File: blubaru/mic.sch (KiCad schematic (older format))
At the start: 8 parts, among them J6 JACK_TRS_6PINS

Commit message: Put parts in the audio switch page.
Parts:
- renumbered C13 to C2, C14 to C3, C15 to C4, C16 to C5, C17 to C6, R9 to R1, R10 to R2
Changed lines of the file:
@@
 MIC_BIAS
 $Comp
-L C C16
+L C C5
 U 1 1 589D21D3
 P 5500 3750
-AR Path="/58AE7D2D/589D21D3" Ref="C16"  Part="1"
-AR Path="/58AEC2DA/58AE7D2D/589D21D3" Ref="C16"  Part="1"
-AR Path="/58B10FE0/58B1273D/58B189CE/58AE7D2D/589D21D3" Ref="C16"  Part="1"
-F 0 "C16" H 5525 3850 50  0000 L CNN
+F 0 "C5" H 5525 3850 50  0000 L CNN
 F 1 "47nF" H 5525 3650 50  0000 L CNN
 F 2 "" H 5538 3600 50  0000 C CNN
@@
 $EndComp
 $Comp
-L C C15
+L C C4
 U 1 1 589D223D
 P 5150 4100
-AR Path="/58AE7D2D/589D223D" Ref="C15"  Part="1"
-AR Path="/58AEC2DA/58AE7D2D/589D223D" Ref="C15"  Part="1"
-AR Path="/58B10FE0/58B1273D/58B189CE/58AE7D2D/589D223D" Ref="C15"  Part="1"
-F 0 "C15" H 5175 4200 50  0000 L CNN
+F 0 "C4" H 5175 4200 50  0000 L CNN
 F 1 "47nF" H 5175 4000 50  0000 L CNN
 F 2 "" H 5188 3950 50  0000 C CNN
@@
 $EndComp
 $Comp
-L C C17
+L C C6
 U 1 1 589D230D
 P 5500 4100
-AR Path="/58AE7D2D/589D230D" Ref="C17"  Part="1"
-AR Path="/58AEC2DA/58AE7D2D/589D230D" Ref="C17"  Part="1"
-AR Path="/58B10FE0/58B1273D/58B189CE/58AE7D2D/589D230D" Ref="C17"  Part="1"
-F 0 "C17" H 5525 4200 50  0000 L CNN
+F 0 "C6" H 5525 4200 50  0000 L CNN
 F 1 "47nF" H 5525 4000 50  0000 L CNN
 F 2 "" H 5538 3950 50  0000 C CNN
@@
 $EndComp
 $Comp
-L C C13
+L C C2
 U 1 1 589D2382
 P 4900 4500
-AR Path="/58AE7D2D/589D2382" Ref="C13"  Part="1"
-AR Path="/58AEC2DA/58AE7D2D/589D2382" Ref="C13"  Part="1"
-AR Path="/58B10FE0/58B1273D/58B189CE/58AE7D2D/589D2382" Ref="C13"  Part="1"
-F 0 "C13" H 4925 4600 50  0000 L CNN
+F 0 "C2" H 4925 4600 50  0000 L CNN
 F 1 "1uF" H 4925 4400 50  0000 L CNN
 F 2 "" H 4938 4350 50  0000 C CNN
@@
 $EndComp
 $Comp
-L C C14
+L C C3
 U 1 1 589D23FA
 P 5150 3650
-AR Path="/58AE7D2D/589D23FA" Ref="C14"  Part="1"
-AR Path="/58AEC2DA/58AE7D2D/589D23FA" Ref="C14"  Part="1"
-AR Path="/58B10FE0/58B1273D/58B189CE/58AE7D2D/589D23FA" Ref="C14"  Part="1"
-F 0 "C14" H 5175 3750 50  0000 L CNN
+F 0 "C3" H 5175 3750 50  0000 L CNN
 F 1 "47nF" H 5175 3550 50  0000 L CNN
 F 2 "" H 5188 3500 50  0000 C CNN
@@
 $EndComp
 $Comp
-L R R9
+L R R1
 U 1 1 589D2492
 P 5750 4000
-AR Path="/58AE7D2D/589D2492" Ref="R9"  Part="1"
-AR Path="/58AEC2DA/58AE7D2D/589D2492" Ref="R9"  Part="1"
-AR Path="/58B10FE0/58B1273D/58B189CE/58AE7D2D/589D2492" Ref="R9"  Part="1"
-F 0 "R9" V 5830 4000 50  0000 C CNN
+F 0 "R1" V 5830 4000 50  0000 C CNN
 F 1 "2k2" V 5750 4000 50  0000 C CNN
 F 2 "" V 5680 4000 50  0000 C CNN
@@
 $EndComp
 $Comp
-L R R10
+L R R2
 U 1 1 589D2525
 P 5950 3950
-AR Path="/58AE7D2D/589D2525" Ref="R10"  Part="1"
-AR Path="/58AEC2DA/58AE7D2D/589D2525" Ref="R10"  Part="1"
-AR Path="/58B10FE0/58B1273D/58B189CE/58AE7D2D/589D2525" Ref="R10"  Part="1"
-F 0 "R10" V 6030 3950 50  0000 C CNN
+F 0 "R2" V 6030 3950 50  0000 C CNN
 F 1 "2k2" V 5950 3950 50  0000 C CNN
 F 2 "" V 5880 3950 50  0000 C CNN
@@
 $EndComp
 $Comp
-L GND #PWR012
+L GND #PWR017
 U 1 1 589D259B
 P 4900 4750
-AR Path="/58AE7D2D/589D259B" Ref="#PWR012"  Part="1"
-AR Path="/58AEC2DA/58AE7D2D/589D259B" Ref="#PWR012"  Part="1"
-AR Path="/58B10FE0/58B1273D/58B189CE/58AE7D2D/589D259B" Ref="#PWR014"  Part="1"
-F 0 "#PWR014" H 4900 4500 50  0001 C CNN
+F 0 "#PWR017" H 4900 4500 50  0001 C CNN
 F 1 "GND" H 4900 4600 50  0000 C CNN
 F 2 "" H 4900 4750 50  0000 C CNN
@@
 U 1 1 589E55E1
 P 6800 3950
-AR Path="/58AE7D2D/589E55E1" Ref="J6"  Part="1"
-AR Path="/58AEC2DA/58AE7D2D/589E55E1" Ref="J6"  Part="1"
-AR Path="/58B10FE0/58B1273D/58B189CE/58AE7D2D/589E55E1" Ref="J6"  Part="1"
 F 0 "J6" H 6800 4350 50  0000 C CNN
 F 1 "JACK_TRS_6PINS" H 6750 3650 50  0000 C CNN
@@
 $EndComp
 $Comp
-L GND #PWR013
+L GND #PWR018
 U 1 1 589E6671
 P 6250 4300
-AR Path="/58AE7D2D/589E6671" Ref="#PWR013"  Part="1"
-AR Path="/58AEC2DA/58AE7D2D/589E6671" Ref="#PWR013"  Part="1"
-AR Path="/58B10FE0/58B1273D/58B189CE/58AE7D2D/589E6671" Ref="#PWR015"  Part="1"
-F 0 "#PWR015" H 6250 4050 50  0001 C CNN
+F 0 "#PWR018" H 6250 4050 50  0001 C CNN
 F 1 "GND" H 6250 4150 50  0000 C CNN
 F 2 "" H 6250 4300 50  0000 C CNN

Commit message: Create footprints for breakout boards
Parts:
- C2, C3, C4, C5, C6: footprint (none) -> Capacitors_THT:C_Disc_D5.0mm_W2.5mm_P2.50mm
- J6: footprint (none) -> Connectors:NMJ6HCD2
- R1, R2: footprint (none) -> Resistors_THT:R_Axial_DIN0207_L6.3mm_D2.5mm_P7.62mm_Horizontal
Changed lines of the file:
@@
 encoding utf-8
 Sheet 7 8
-Title ""
-Date ""
+Title "Blubaru"
+Date "2017-02-28"
 Rev ""
 Comp ""
@@
 F 0 "C5" H 5525 3850 50  0000 L CNN
 F 1 "47nF" H 5525 3650 50  0000 L CNN
-F 2 "" H 5538 3600 50  0000 C CNN
+F 2 "Capacitors_THT:C_Disc_D5.0mm_W2.5mm_P2.50mm" H 5538 3600 50  0001 C CNN
 F 3 "" H 5500 3750 50  0000 C CNN
 	1    5500 3750
@@
 F 0 "C4" H 5175 4200 50  0000 L CNN
 F 1 "47nF" H 5175 4000 50  0000 L CNN
-F 2 "" H 5188 3950 50  0000 C CNN
+F 2 "Capacitors_THT:C_Disc_D5.0mm_W2.5mm_P2.50mm" H 5188 3950 50  0001 C CNN
 F 3 "" H 5150 4100 50  0000 C CNN
 	1    5150 4100
@@
 F 0 "C6" H 5525 4200 50  0000 L CNN
 F 1 "47nF" H 5525 4000 50  0000 L CNN
-F 2 "" H 5538 3950 50  0000 C CNN
+F 2 "Capacitors_THT:C_Disc_D5.0mm_W2.5mm_P2.50mm" H 5538 3950 50  0001 C CNN
 F 3 "" H 5500 4100 50  0000 C CNN
 	1    5500 4100
@@
 F 0 "C2" H 4925 4600 50  0000 L CNN
 F 1 "1uF" H 4925 4400 50  0000 L CNN
-F 2 "" H 4938 4350 50  0000 C CNN
+F 2 "Capacitors_THT:C_Disc_D5.0mm_W2.5mm_P2.50mm" H 4938 4350 50  0001 C CNN
 F 3 "" H 4900 4500 50  0000 C CNN
 	1    4900 4500
@@
 F 0 "C3" H 5175 3750 50  0000 L CNN
 F 1 "47nF" H 5175 3550 50  0000 L CNN
-F 2 "" H 5188 3500 50  0000 C CNN
+F 2 "Capacitors_THT:C_Disc_D5.0mm_W2.5mm_P2.50mm" H 5188 3500 50  0001 C CNN
 F 3 "" H 5150 3650 50  0000 C CNN
 	1    5150 3650
@@
 F 0 "R1" V 5830 4000 50  0000 C CNN
 F 1 "2k2" V 5750 4000 50  0000 C CNN
-F 2 "" V 5680 4000 50  0000 C CNN
+F 2 "Resistors_THT:R_Axial_DIN0207_L6.3mm_D2.5mm_P7.62mm_Horizontal" V 5680 4000 50  0001 C CNN
 F 3 "" H 5750 4000 50  0000 C CNN
 	1    5750 4000
@@
 F 0 "R2" V 6030 3950 50  0000 C CNN
 F 1 "2k2" V 5950 3950 50  0000 C CNN
-F 2 "" V 5880 3950 50  0000 C CNN
+F 2 "Resistors_THT:R_Axial_DIN0207_L6.3mm_D2.5mm_P7.62mm_Horizontal" V 5880 3950 50  0001 C CNN
 F 3 "" H 5950 3950 50  0000 C CNN
 	1    5950 3950
@@
 $EndComp
 $Comp
-L GND #PWR017
+L GND #PWR020
 U 1 1 589D259B
 P 4900 4750
-F 0 "#PWR017" H 4900 4500 50  0001 C CNN
+F 0 "#PWR020" H 4900 4500 50  0001 C CNN
 F 1 "GND" H 4900 4600 50  0000 C CNN
 F 2 "" H 4900 4750 50  0000 C CNN
@@
 F 0 "J6" H 6800 4350 50  0000 C CNN
 F 1 "JACK_TRS_6PINS" H 6750 3650 50  0000 C CNN
-F 2 "" H 6900 3800 50  0000 C CNN
+F 2 "Connectors:NMJ6HCD2" H 6900 3800 50  0001 C CNN
 F 3 "" H 6900 3800 50  0000 C CNN
 	1    6800 3950
@@
 $EndComp
 $Comp
-L GND #PWR018
+L GND #PWR021
 U 1 1 589E6671
 P 6250 4300
-F 0 "#PWR018" H 6250 4050 50  0001 C CNN
+F 0 "#PWR021" H 6250 4050 50  0001 C CNN
 F 1 "GND" H 6250 4150 50  0000 C CNN
 F 2 "" H 6250 4300 50  0000 C CNN

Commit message: Update footprints for passives.
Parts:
- R1, R2: footprint Resistors_THT:R_Axial_DIN0207_L6.3mm_D2.5mm_P7.62mm_Horizontal -> Resistors_THT:R_Axial_DIN0204_L3.6mm_D1.6mm_P5.08mm_Horizontal
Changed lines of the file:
@@
 F 0 "R1" V 5830 4000 50  0000 C CNN
 F 1 "2k2" V 5750 4000 50  0000 C CNN
-F 2 "Resistors_THT:R_Axial_DIN0207_L6.3mm_D2.5mm_P7.62mm_Horizontal" V 5680 4000 50  0001 C CNN
+F 2 "Resistors_THT:R_Axial_DIN0204_L3.6mm_D1.6mm_P5.08mm_Horizontal" V 5680 4000 50  0001 C CNN
 F 3 "" H 5750 4000 50  0000 C CNN
 	1    5750 4000
@@
 F 0 "R2" V 6030 3950 50  0000 C CNN
 F 1 "2k2" V 5950 3950 50  0000 C CNN
-F 2 "Resistors_THT:R_Axial_DIN0207_L6.3mm_D2.5mm_P7.62mm_Horizontal" V 5880 3950 50  0001 C CNN
+F 2 "Resistors_THT:R_Axial_DIN0204_L3.6mm_D1.6mm_P5.08mm_Horizontal" V 5880 3950 50  0001 C CNN
 F 3 "" H 5950 3950 50  0000 C CNN
 	1    5950 3950

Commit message: Added footprint for audio jack.
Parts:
- J6: footprint Connectors:NMJ6HCD2 -> blubaru:SJ1-3523NG
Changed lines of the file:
@@
 F 0 "J6" H 6800 4350 50  0000 C CNN
 F 1 "JACK_TRS_6PINS" H 6750 3650 50  0000 C CNN
-F 2 "Connectors:NMJ6HCD2" H 6900 3800 50  0001 C CNN
+F 2 "blubaru:SJ1-3523NG" H 6900 3800 50  0001 C CNN
 F 3 "" H 6900 3800 50  0000 C CNN
 	1    6800 3950

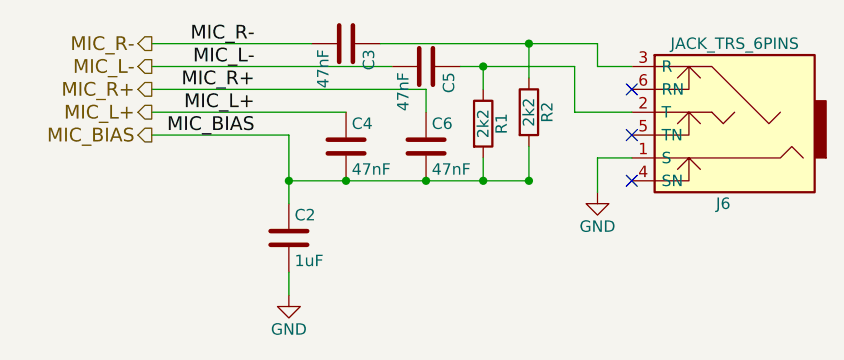
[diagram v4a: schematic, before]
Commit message: Add a new 5-pin jack to schematic library and use it.
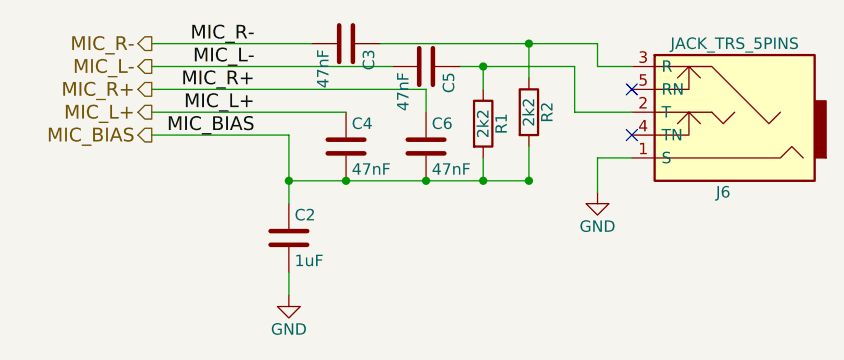
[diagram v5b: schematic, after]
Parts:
- removed J6: JACK_TRS_6PINS, blubaru:SJ1-3523NG, symbol JACK_TRS_6PINS
- added J6: JACK_TRS_5PINS, symbol JACK_TRS_5PINS
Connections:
- net GND: now also J6.1 (S)
- net at C5.1, R1.1: now also J6.2 (T)
- net at C3.1, R2.1: now also J6.3 (R)
- no-connect marks 3 -> 2
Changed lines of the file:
@@
-$EndComp
-$Comp
-L JACK_TRS_6PINS J6
-U 1 1 589E55E1
-P 6800 3950
-F 0 "J6" H 6800 4350 50  0000 C CNN
-F 1 "JACK_TRS_6PINS" H 6750 3650 50  0000 C CNN
-F 2 "blubaru:SJ1-3523NG" H 6900 3800 50  0001 C CNN
-F 3 "" H 6900 3800 50  0000 C CNN
-	1    6800 3950
-	-1   0    0    1
 $EndComp
 $Comp
@@
 NoConn ~ 6400 3850
 NoConn ~ 6400 4050
-NoConn ~ 6400 4250
 Text HLabel 4300 3650 0    60   Output ~ 0
 MIC_R-
@@
 Text HLabel 4300 4050 0    60   Output ~ 0
 MIC_BIAS
+$Comp
+L JACK_TRS_5PINS J6
+U 1 1 58BF91C1
+P 6800 3950
+F 0 "J6" H 6800 4300 50  0000 C CNN
+F 1 "JACK_TRS_5PINS" H 6750 3650 50  0000 C CNN
+F 2 "" H 6900 3800 50  0001 C CNN
+F 3 "" H 6900 3800 50  0001 C CNN
+	1    6800 3950
+	-1   0    0    1
+$EndComp
 $EndSCHEMATC

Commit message: re-pair new 5-pin jack with footprint
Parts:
- J6: footprint (none) -> blubaru:SJ1-3523NG
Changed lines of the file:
@@
 F 0 "J6" H 6800 4300 50  0000 C CNN
 F 1 "JACK_TRS_5PINS" H 6750 3650 50  0000 C CNN
-F 2 "" H 6900 3800 50  0001 C CNN
+F 2 "blubaru:SJ1-3523NG" H 6900 3800 50  0001 C CNN
 F 3 "" H 6900 3800 50  0001 C CNN
 	1    6800 3950
